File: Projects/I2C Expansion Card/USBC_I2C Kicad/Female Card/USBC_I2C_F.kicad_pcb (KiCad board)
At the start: 2 copper layers, 26 x 30 mm, 11 parts, among them U1 MCP2221AxSL

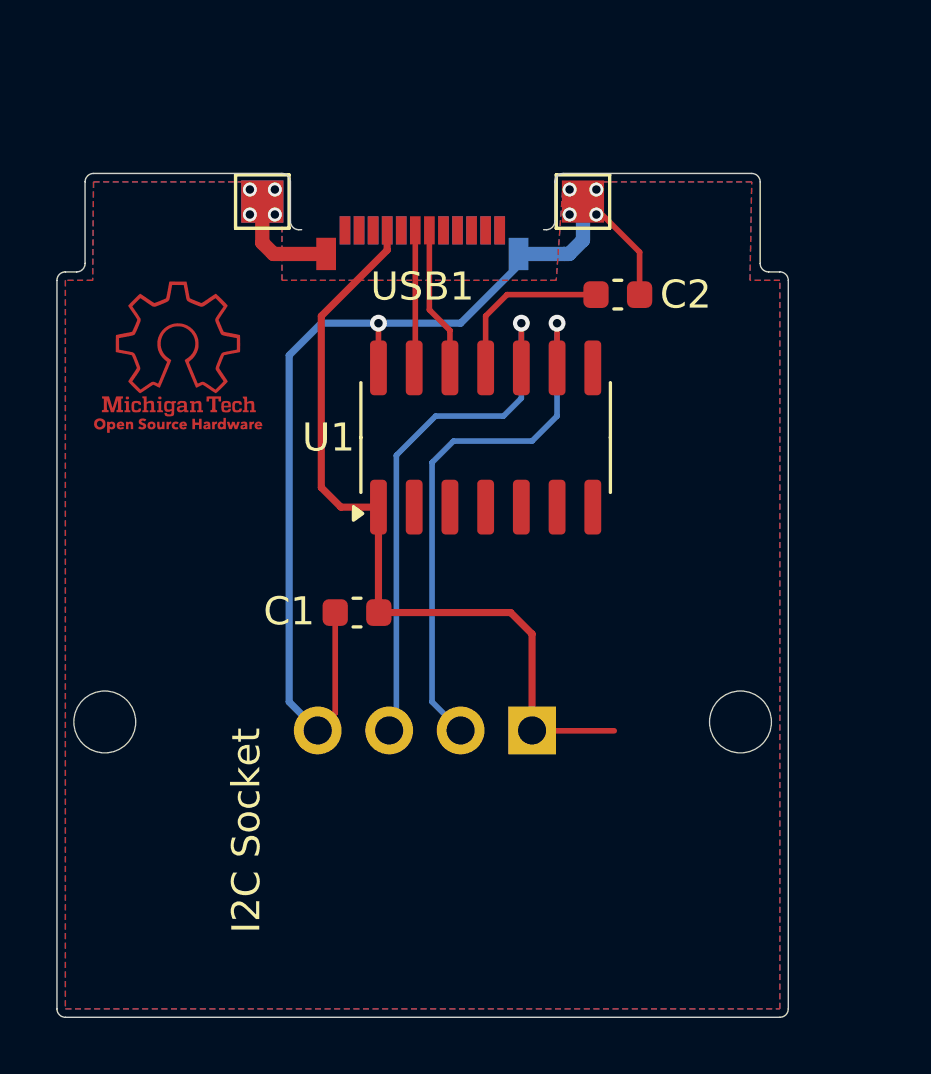
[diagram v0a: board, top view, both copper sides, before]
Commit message: Added Impedance Matching and added 5V Plane
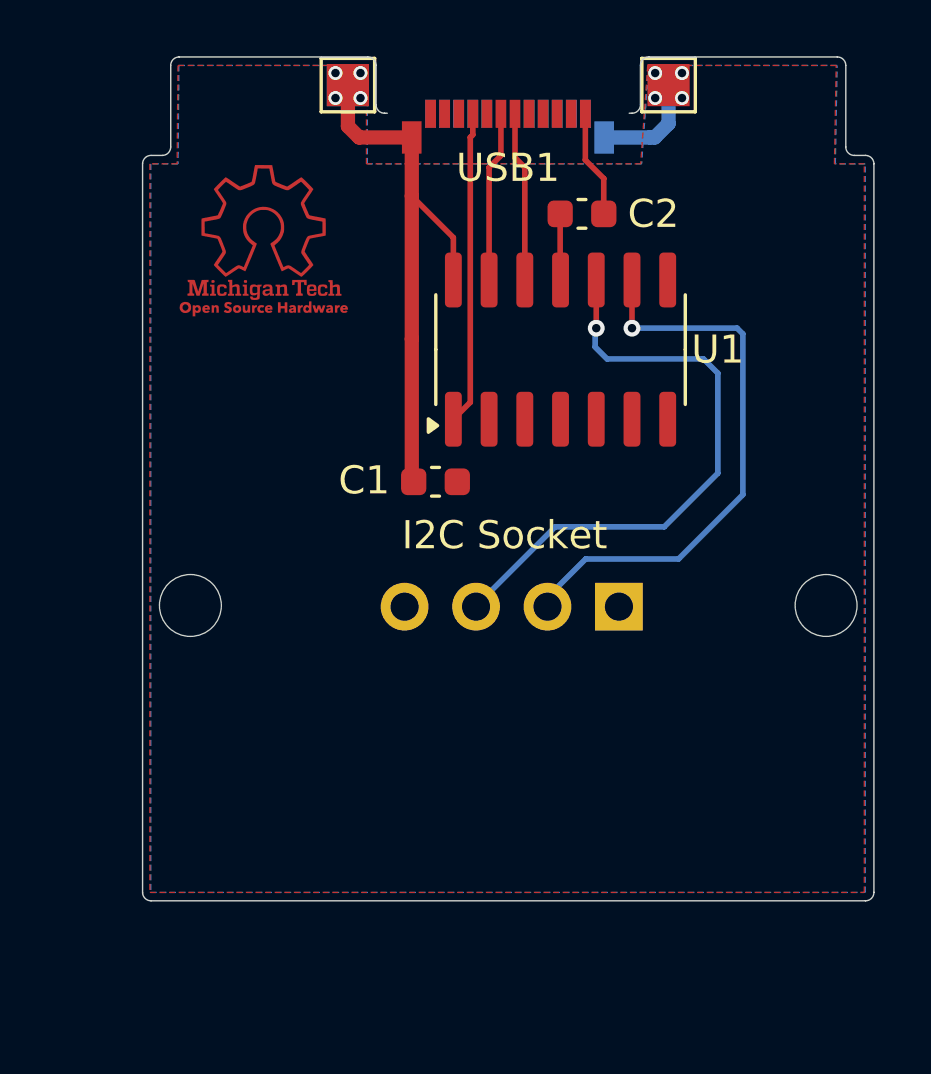
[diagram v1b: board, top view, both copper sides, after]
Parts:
- moved C1 5.42 mm to (97.3, 68.1), turned to 180 degrees
- moved I2C Socket 5.38 mm to (103.8, 72.6)
- moved USB1 5.14 mm to (99.9, 55.0)
- moved H1 5.14 mm to (88.6, 72.5)
- moved TP3 5.14 mm to (105.6, 54.0)
- moved G*** 5.14 mm to (91.2, 59.6)
- moved H2 5.14 mm to (111.2, 72.5)
- moved TP1 5.14 mm to (94.2, 54.0)
- moved TP2 5.14 mm to (94.2, 54.0)
- moved U1 4.11 mm to (101.7, 63.4)
- moved C2 3.14 mm to (102.5, 58.6)
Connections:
- C1 pad 1: GND -> 5V
- C1 pad 2: 5V -> GND
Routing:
- net 5V: track 28.1 -> 11.1 mm
- net GND: track 41.9 -> 27.7 mm, vias 9 -> 8
- net Net-(U1-VUSB): track 6.08 -> 2.36 mm
- net SCL: track 19.4 -> 21.5 mm
- net Net-(U1-D+): track 4.91 -> 6.08 mm
- net Net-(U1-D-): track 5.19 -> 6.05 mm
- added copper zone on F.Cu, net 5V
- removed copper zone on F.Cu, net GND
